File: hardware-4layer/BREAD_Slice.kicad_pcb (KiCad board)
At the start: 4 copper layers, 70 x 100 mm, 16 parts, among them J1 Conn_01x10_Female, U1 AP63205

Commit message: added 4L-XL tempalte
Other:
- board text added: "L1 (Top): - Template digital components (Nano, RGB LED) and I²C signals - use minimal ground pours. L2 (Inner 1): - Solid ground plane - split into an upper {dblquote}gndpwr{dblquote} zone (handling 12V returns) and a lower digital ground zone, connected only at the regulator - these can be resized to accommadate additional planes i.e. decreasing 12V/GNDPWR planes to connector edge and creating a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"
- board text removed: "L1 (Top):Template digital components (Nano, RGB LED) and I²C signals; minimal ground pours. L2 (Inner 1): Solid ground plane; split into an upper {dblquote}gndpwr{dblquote} zone (handling 12V returns) and a lower digital ground zone, connected only at the regulator. L3 (Inner 2): Dedicated power plane; upper zone for 12V, lower zone for 5V, kept separate until the regulator. L4 (Bottom): Secondar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"
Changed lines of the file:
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@@
 		)
 	)
-	(gr_text "L1 (Top):Template digital components (Nano, RGB LED) and I²C signals; minimal ground pours.\n\nL2 (Inner 1): Solid ground plane; split into an upper {dblquote}gndpwr{dblquote} zone (handling 12V returns) and a lower digital ground zone, connected only at the regulator.\n\nL3 (Inner 2): Dedicated power plane; upper zone for 12V, lower zone for 5V, kept separate until the regulator.\n\nL4 (Bottom): Secondary signal routing; minimal pours, with localized copper such as the templates regulator."
-		(at 95.675 156.675 0)
+	(gr_text "L1 (Top):\n	- Template digital components (Nano, RGB LED) and I²C signals\n	- use minimal ground pours.\n\nL2 (Inner 1): \n	- Solid ground plane\n	- split into an upper {dblquote}gndpwr{dblquote} zone (handling 12V returns) and a lower digital ground zone, connected only at the regulator\n	- these can be resized to accommadate additional planes i.e. decreasing 12V/GNDPWR planes to connector edge and creating analog plane\n\nL3 (Inner 2):\n	- Dedicated power plane\n	- upper zone for 12V, lower zone for 5V, kept separate until the regulator.\n	- same as L2, can be resized to accomadate additional planes\n\nL4 (Bottom):\n	- Secondary signal routing; minimal pours, with localized copper such as the templates regulator."
+		(at 96.27 176.19 0)
 		(layer "Cmts.User")
 		(effects

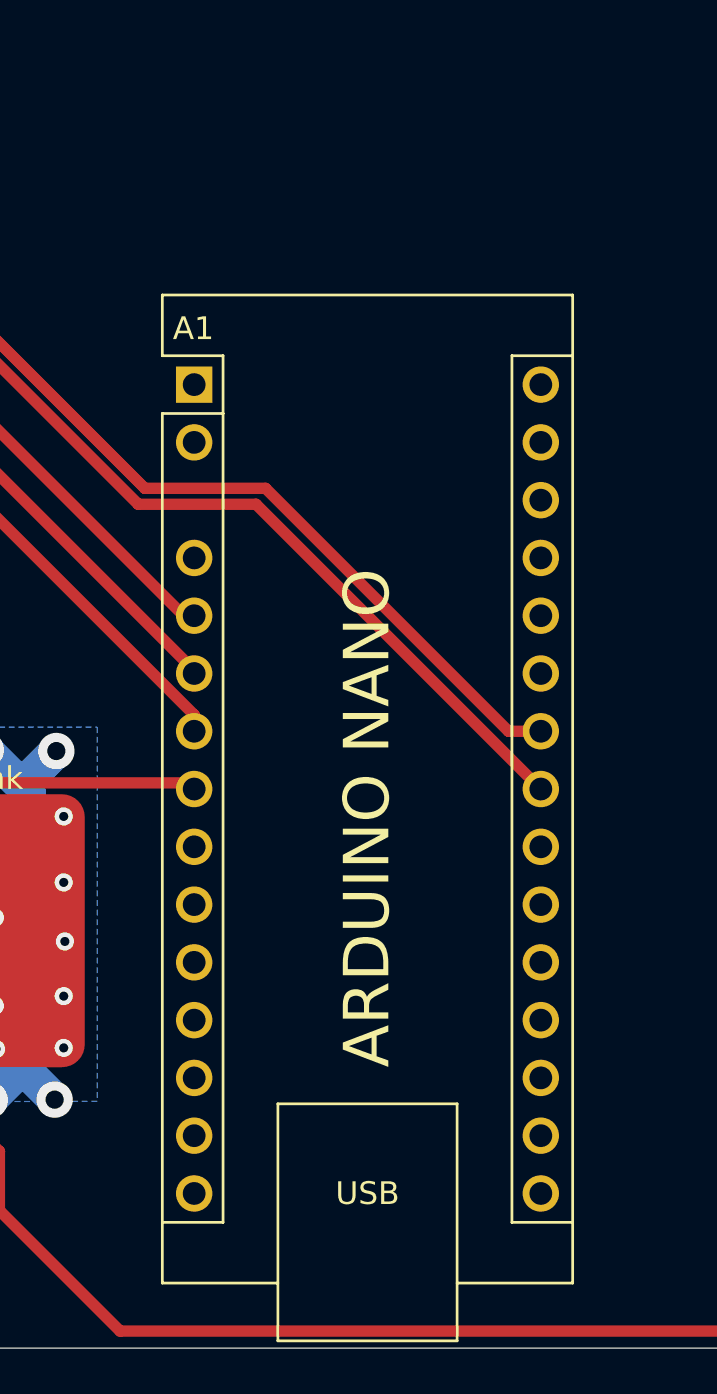
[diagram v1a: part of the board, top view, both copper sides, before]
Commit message: updated 4 layer tempalte
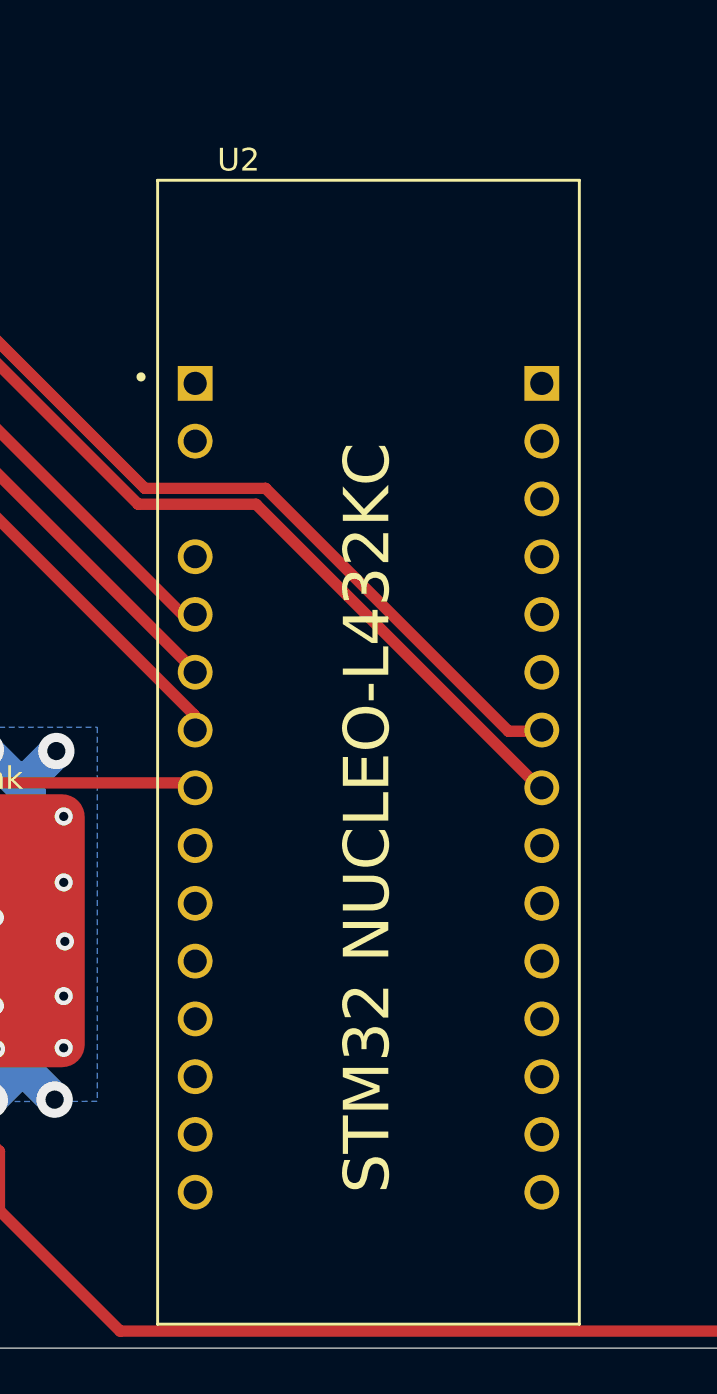
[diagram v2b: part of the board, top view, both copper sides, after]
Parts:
- removed A1: Arduino_Nano_v3.x, Module:Arduino_Nano
- added U2: NUCLEO-L432KC, kml-custom:MODULE_NUCLEO-L432KC, F.Cu at (124.1, 107.4)
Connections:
- net +5V renamed +5VD
- net GND renamed GNDD
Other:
- board text added: "STM32 NUCLEO-L432KC"
- board text removed: "ARDUINO NANO"
